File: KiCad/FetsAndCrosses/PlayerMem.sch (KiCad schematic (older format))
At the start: 0 parts

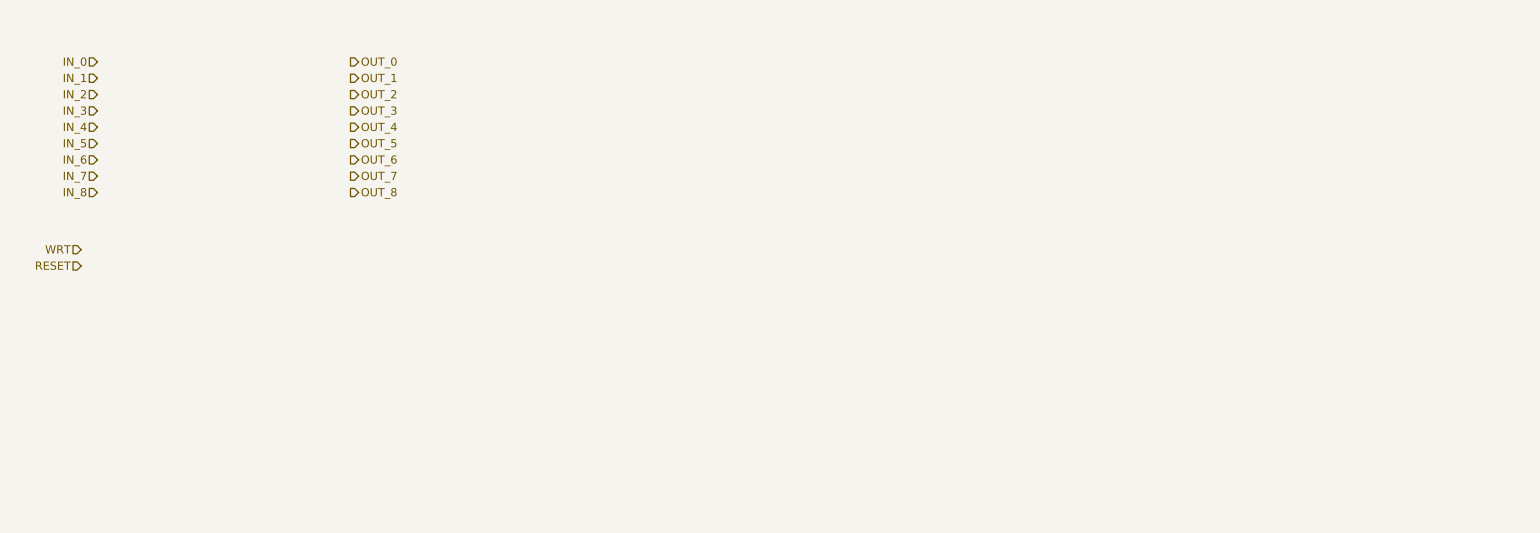
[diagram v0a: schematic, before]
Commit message: Reworked everything to use Buses
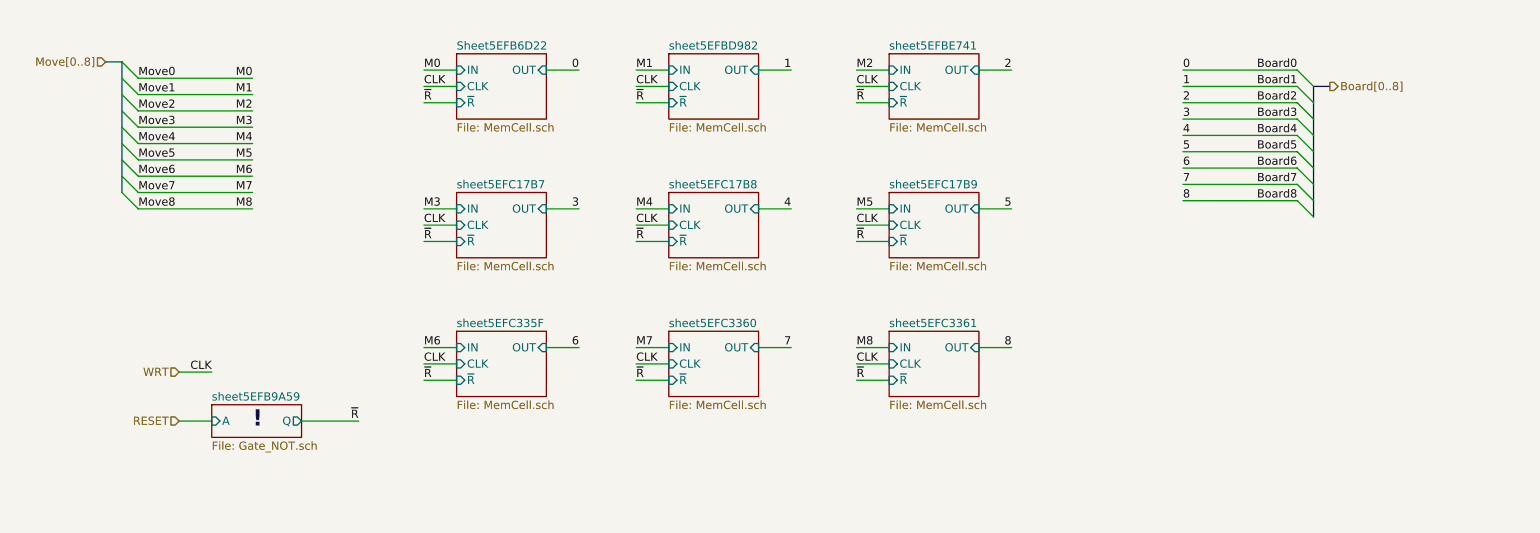
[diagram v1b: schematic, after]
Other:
- note added: "!"

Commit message: Schematic Done, Footprints assigned, ERC OK.
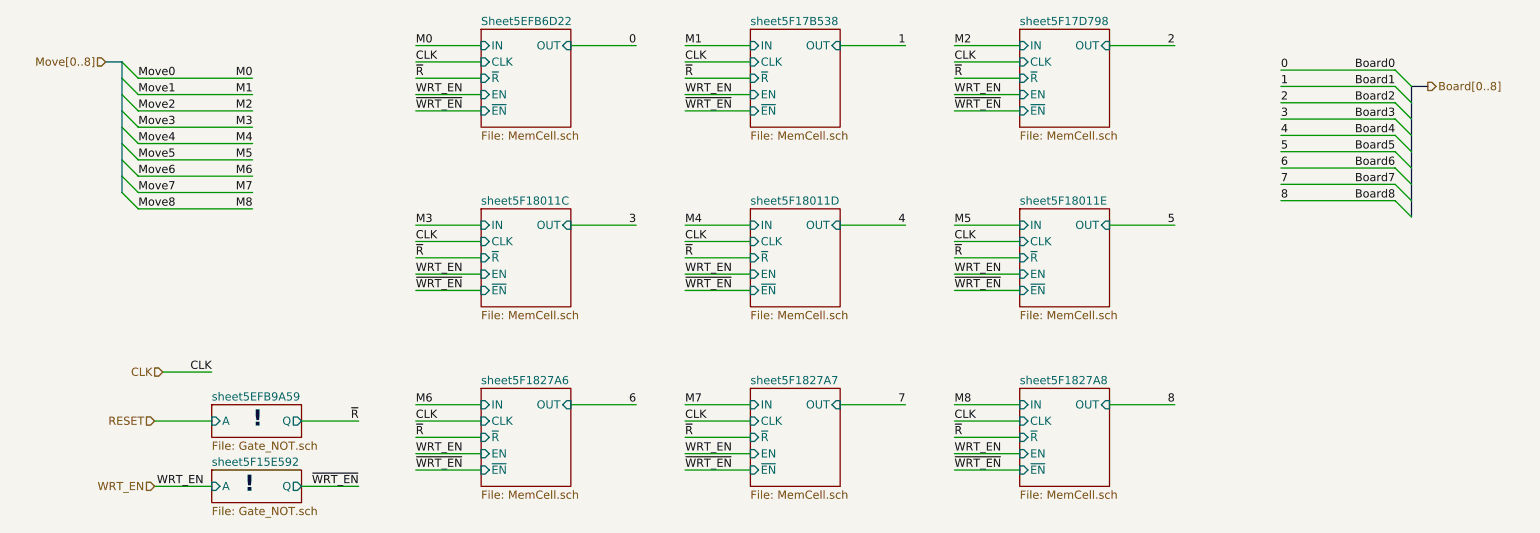
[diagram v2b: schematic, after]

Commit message: First Draft Schematic Updates
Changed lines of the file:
@@
 $Descr A4 11693 8268
 encoding utf-8
-Sheet 262 389
+Sheet 2 360
 Title ""
 Date "2020-07-05"
@@
 $EndSheet
 $Sheet
-S 2600 3850 550  200
-U 5F15E596
-F0 "sheet5F15E592" 50
-F1 "Gate_NOT.sch" 50
-F2 "A" I L 2600 3950 50
-F3 "Q" O R 3150 3950 50
-$EndSheet
-$Sheet
 S 4250 1150 550  600
 U 5EFB6D23
@@
 F5 "OUT" I R 4800 1250 50
 F6 "EN" I L 4250 1550 50
-F7 "~EN" I L 4250 1650 50
 $EndSheet
 $Sheet
@@
 F5 "OUT" I R 6450 1250 50
 F6 "EN" I L 5900 1550 50
-F7 "~EN" I L 5900 1650 50
 $EndSheet
 $Sheet
@@
 F5 "OUT" I R 8100 1250 50
 F6 "EN" I L 7550 1550 50
-F7 "~EN" I L 7550 1650 50
 $EndSheet
 $Sheet
@@
 F5 "OUT" I R 4800 2350 50
 F6 "EN" I L 4250 2650 50
-F7 "~EN" I L 4250 2750 50
 $EndSheet
 $Sheet
@@
 F5 "OUT" I R 6450 2350 50
 F6 "EN" I L 5900 2650 50
-F7 "~EN" I L 5900 2750 50
 $EndSheet
 $Sheet
@@
 F5 "OUT" I R 8100 2350 50
 F6 "EN" I L 7550 2650 50
-F7 "~EN" I L 7550 2750 50
 $EndSheet
 $Sheet
@@
 F5 "OUT" I R 4800 3450 50
 F6 "EN" I L 4250 3750 50
-F7 "~EN" I L 4250 3850 50
 $EndSheet
 $Sheet
@@
 F5 "OUT" I R 6450 3450 50
 F6 "EN" I L 5900 3750 50
-F7 "~EN" I L 5900 3850 50
 $EndSheet
 $Sheet
@@
 F5 "OUT" I R 8100 3450 50
 F6 "EN" I L 7550 3750 50
-F7 "~EN" I L 7550 3850 50
 $EndSheet
 Text HLabel 2300 3250 0    50   Input ~ 0
@@
 Text Label 2600 3250 2    50   ~ 0
 CLK
-Text HLabel 2250 3950 0    50   Input ~ 0
-WRT_EN
-Text Label 2550 3950 2    50   ~ 0
-WRT_EN
-Text Notes 2800 4000 0    100  ~ 20
-!
-Text Label 3500 3950 2    50   ~ 0
-~WRT_EN
+Text HLabel 2350 3900 0    50   Input ~ 0
+WRT_EN
+Text Label 2700 3900 2    50   ~ 0
+WRT_EN
 Text Label 3850 1350 0    50   ~ 0
 CLK
 Text Label 3850 1450 0    50   ~ 0
 ~R
-Text Label 3850 1650 0    50   ~ 0
-~WRT_EN
 Text Label 3850 1550 0    50   ~ 0
 WRT_EN
@@
 Text Label 5500 1450 0    50   ~ 0
 ~R
-Text Label 5500 1650 0    50   ~ 0
-~WRT_EN
 Text Label 5500 1550 0    50   ~ 0
 WRT_EN
@@
 Text Label 7150 1450 0    50   ~ 0
 ~R
-Text Label 7150 1650 0    50   ~ 0
-~WRT_EN
 Text Label 7150 1550 0    50   ~ 0
 WRT_EN
@@
 Text Label 3850 2550 0    50   ~ 0
 ~R
-Text Label 3850 2750 0    50   ~ 0
-~WRT_EN
 Text Label 3850 2650 0    50   ~ 0
 WRT_EN
@@
 Text Label 5500 2550 0    50   ~ 0
 ~R
-Text Label 5500 2750 0    50   ~ 0
-~WRT_EN
 Text Label 5500 2650 0    50   ~ 0
 WRT_EN
@@
 Text Label 7150 2550 0    50   ~ 0
 ~R
-Text Label 7150 2750 0    50   ~ 0
-~WRT_EN
 Text Label 7150 2650 0    50   ~ 0
 WRT_EN
@@
 Text Label 3850 3650 0    50   ~ 0
 ~R
-Text Label 3850 3850 0    50   ~ 0
-~WRT_EN
 Text Label 3850 3750 0    50   ~ 0
 WRT_EN
@@
 Text Label 5500 3650 0    50   ~ 0
 ~R
-Text Label 5500 3850 0    50   ~ 0
-~WRT_EN
 Text Label 5500 3750 0    50   ~ 0
 WRT_EN
@@
 Text Label 7150 3650 0    50   ~ 0
 ~R
-Text Label 7150 3850 0    50   ~ 0
-~WRT_EN
 Text Label 7150 3750 0    50   ~ 0
 WRT_EN
@@
 	2300 3250 2600 3250
 Wire Wire Line
-	2250 3950 2600 3950
-Wire Wire Line
-	3150 3950 3500 3950
+	2350 3900 2700 3900
 Wire Wire Line
 	4250 1450 3850 1450
@@
 	3850 1550 4250 1550
 Wire Wire Line
-	3850 1650 4250 1650
-Wire Wire Line
 	4250 1350 3850 1350
 Wire Wire Line
@@
 	5500 1550 5900 1550
 Wire Wire Line
-	5500 1650 5900 1650
-Wire Wire Line
 	5900 1350 5500 1350
 Wire Wire Line
@@
 	7150 1550 7550 1550
 Wire Wire Line
-	7150 1650 7550 1650
-Wire Wire Line
 	7550 1350 7150 1350
 Wire Wire Line
@@
 	3850 2650 4250 2650
 Wire Wire Line
-	3850 2750 4250 2750
-Wire Wire Line
 	4250 2450 3850 2450
 Wire Wire Line
@@
 	5500 2650 5900 2650
 Wire Wire Line
-	5500 2750 5900 2750
-Wire Wire Line
 	5900 2450 5500 2450
 Wire Wire Line
@@
 	7150 2650 7550 2650
 Wire Wire Line
-	7150 2750 7550 2750
-Wire Wire Line
 	7550 2450 7150 2450
 Wire Wire Line
@@
 	3850 3750 4250 3750
 Wire Wire Line
-	3850 3850 4250 3850
-Wire Wire Line
 	4250 3550 3850 3550
 Wire Wire Line
@@
 	5500 3750 5900 3750
 Wire Wire Line
-	5500 3850 5900 3850
-Wire Wire Line
 	5900 3550 5500 3550
 Wire Wire Line
@@
 	7150 3750 7550 3750
 Wire Wire Line
-	7150 3850 7550 3850
-Wire Wire Line
 	7550 3550 7150 3550
